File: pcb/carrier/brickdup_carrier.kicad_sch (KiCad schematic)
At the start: 29 parts, among them J1 VBAT IN (JST PH), SW1 PWR SWITCH (JST PH), U1 MP9486A

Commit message: pcb: carrier Cff footprint 0402 -> 0603 for hand-rework
Cff is the designated bench-tuning part (hysteretic ripple injection); 0603
matches the cap kit and human hands. Re-placed + re-routed, DRC 0/0.

Co-Authored-By: Claude Fable 5 <noreply@anthropic.com>
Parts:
- Cff: footprint Capacitor_SMD:C_0402_1005Metric -> Capacitor_SMD:C_0603_1608Metric
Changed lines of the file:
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@@
     (property "Reference" "Cff" (at 232.41 63.49999999999999 0) (effects (font (size 1.27 1.27)) (justify left)))
     (property "Value" "470pF" (at 232.41 66.03999999999999 0) (effects (font (size 1.27 1.27)) (justify left)))
-    (property "Footprint" "Capacitor_SMD:C_0402_1005Metric" (at 229.87 64.77 0) (effects (font (size 1.27 1.27)) (hide yes)))
+    (property "Footprint" "Capacitor_SMD:C_0603_1608Metric" (at 229.87 64.77 0) (effects (font (size 1.27 1.27)) (hide yes)))
     (property "Datasheet" "" (at 229.87 64.77 0) (effects (font (size 1.27 1.27)) (hide yes)))
     (pin "1")

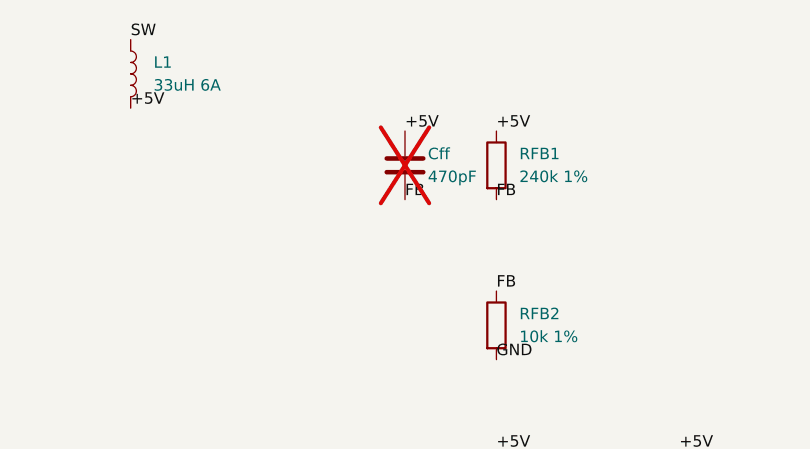
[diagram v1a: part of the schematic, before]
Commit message: pcb: carrier Cff populated by default (470pF 0603, machine-placed)
Zero-hand-SMD build goal: all 24 SMT parts machine-placed incl. Cff; sockets
via JLC THT/hand-solder service (8.5mm height noted); JST wire-loop plug
documented as the solderless SW1 bypass.

Co-Authored-By: Claude Fable 5 <noreply@anthropic.com>
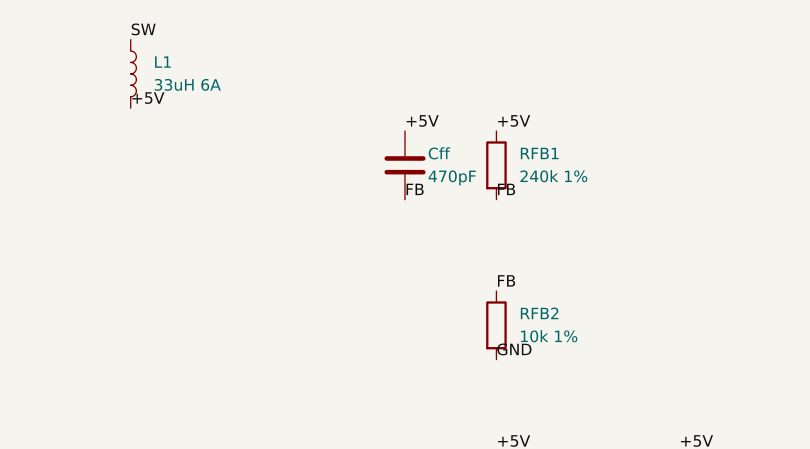
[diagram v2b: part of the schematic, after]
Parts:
- Cff: now fitted
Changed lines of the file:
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@@
     (at 229.87 64.77 0)
     (unit 1)
-    (exclude_from_sim no) (in_bom yes) (on_board yes) (dnp yes)
+    (exclude_from_sim no) (in_bom yes) (on_board yes) (dnp no)
     (property "Reference" "Cff" (at 232.41 63.49999999999999 0) (effects (font (size 1.27 1.27)) (justify left)))
     (property "Value" "470pF" (at 232.41 66.03999999999999 0) (effects (font (size 1.27 1.27)) (justify left)))

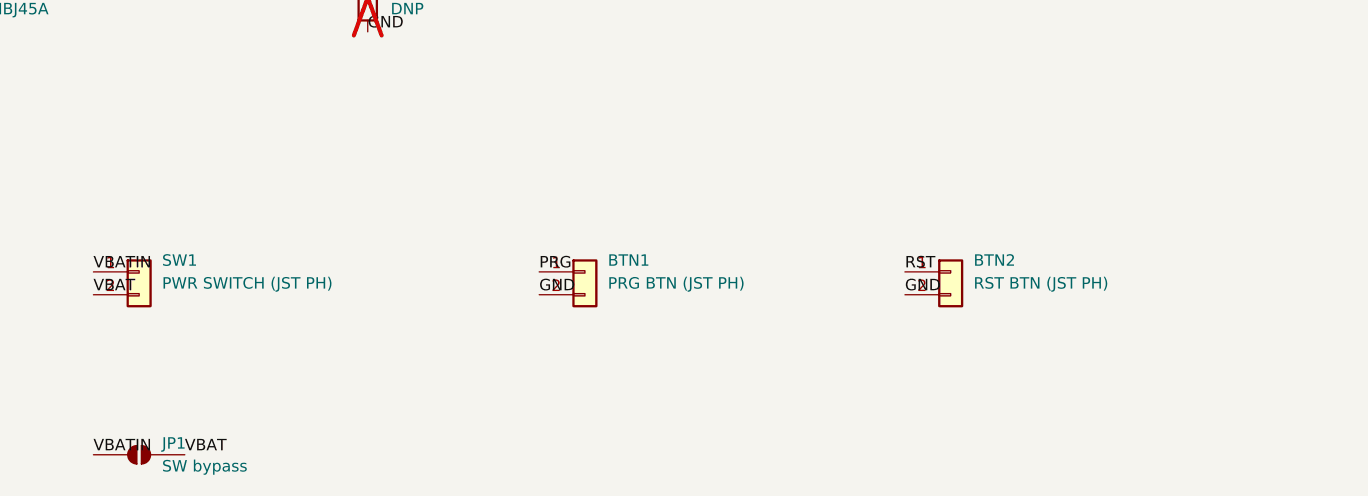
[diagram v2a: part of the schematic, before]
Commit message: pcb: SW1/BTN1/BTN2 -> vertical THT JST (B2B-PH-K-S, C131337)
Top-entry wire exit suits the enclosure (button wires run up to lid
flexures), THT legs are strongest for plug cycles, part is genuine JST,
in stock, and rides the same hand-solder line as the sockets. J1 stays
side-entry facing the LEMO wall. Clip access verified: >=2mm to every
neighbour (BTN2 nudged off the BRK1 row), all fully on-board (edge
exemption now J1 only). Re-routed, DRC 0/0, layout rules pass, full fab
package regenerated (gerbers/BOM/CPL).

Co-Authored-By: Claude Fable 5 <noreply@anthropic.com>
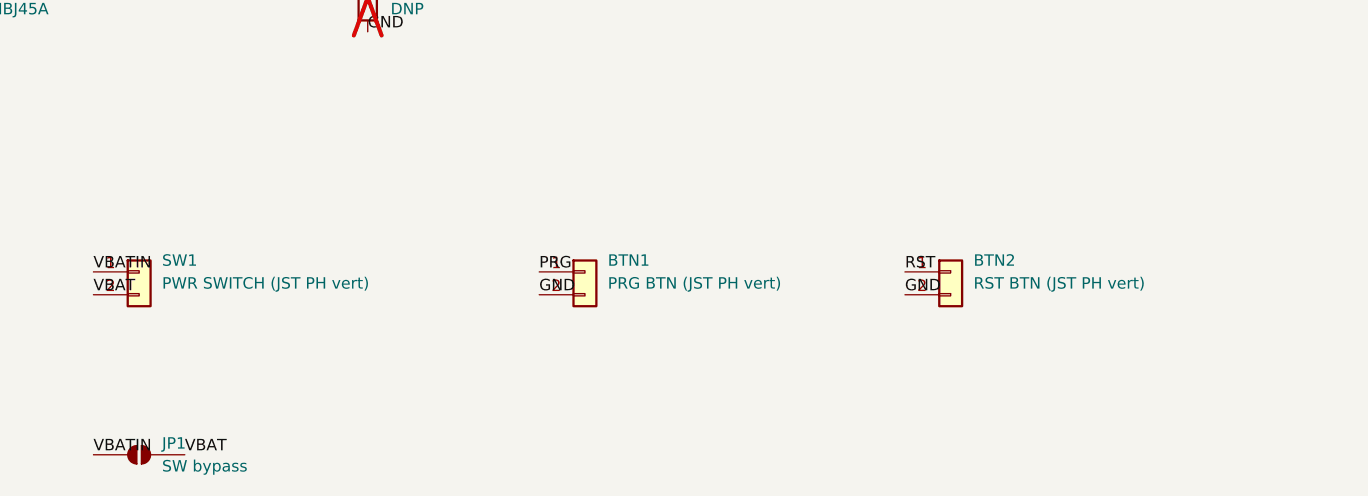
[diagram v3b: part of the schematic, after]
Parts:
- BTN1: value PRG BTN (JST PH) -> PRG BTN (JST PH vert); footprint Connector_JST:JST_PH_S2B-PH-SM4-TB_1x02-1MP_P2.00mm_Horizontal -> Connector_JST:JST_PH_B2B-PH-K_1x02_P2.00mm_Vertical
- BTN2: value RST BTN (JST PH) -> RST BTN (JST PH vert); footprint Connector_JST:JST_PH_S2B-PH-SM4-TB_1x02-1MP_P2.00mm_Horizontal -> Connector_JST:JST_PH_B2B-PH-K_1x02_P2.00mm_Vertical
- SW1: value PWR SWITCH (JST PH) -> PWR SWITCH (JST PH vert); footprint Connector_JST:JST_PH_S2B-PH-SM4-TB_1x02-1MP_P2.00mm_Horizontal -> Connector_JST:JST_PH_B2B-PH-K_1x02_P2.00mm_Vertical
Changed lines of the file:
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@@
     (exclude_from_sim no) (in_bom yes) (on_board yes) (dnp no)
     (property "Reference" "SW1" (at 82.55000000000001 158.75 0) (effects (font (size 1.27 1.27)) (justify left)))
-    (property "Value" "PWR SWITCH (JST PH)" (at 82.55000000000001 161.29000000000002 0) (effects (font (size 1.27 1.27)) (justify left)))
-    (property "Footprint" "Connector_JST:JST_PH_S2B-PH-SM4-TB_1x02-1MP_P2.00mm_Horizontal" (at 80.01 160.02 0) (effects (font (size 1.27 1.27)) (hide yes)))
+    (property "Value" "PWR SWITCH (JST PH vert)" (at 82.55000000000001 161.29000000000002 0) (effects (font (size 1.27 1.27)) (justify left)))
+    (property "Footprint" "Connector_JST:JST_PH_B2B-PH-K_1x02_P2.00mm_Vertical" (at 80.01 160.02 0) (effects (font (size 1.27 1.27)) (hide yes)))
     (property "Datasheet" "" (at 80.01 160.02 0) (effects (font (size 1.27 1.27)) (hide yes)))
     (pin "1")
@@
     (exclude_from_sim no) (in_bom yes) (on_board yes) (dnp no)
     (property "Reference" "BTN1" (at 132.07999999999998 158.75 0) (effects (font (size 1.27 1.27)) (justify left)))
-    (property "Value" "PRG BTN (JST PH)" (at 132.07999999999998 161.29000000000002 0) (effects (font (size 1.27 1.27)) (justify left)))
-    (property "Footprint" "Connector_JST:JST_PH_S2B-PH-SM4-TB_1x02-1MP_P2.00mm_Horizontal" (at 129.54 160.02 0) (effects (font (size 1.27 1.27)) (hide yes)))
+    (property "Value" "PRG BTN (JST PH vert)" (at 132.07999999999998 161.29000000000002 0) (effects (font (size 1.27 1.27)) (justify left)))
+    (property "Footprint" "Connector_JST:JST_PH_B2B-PH-K_1x02_P2.00mm_Vertical" (at 129.54 160.02 0) (effects (font (size 1.27 1.27)) (hide yes)))
     (property "Datasheet" "" (at 129.54 160.02 0) (effects (font (size 1.27 1.27)) (hide yes)))
     (pin "1")
@@
     (exclude_from_sim no) (in_bom yes) (on_board yes) (dnp no)
     (property "Reference" "BTN2" (at 172.72 158.75 0) (effects (font (size 1.27 1.27)) (justify left)))
-    (property "Value" "RST BTN (JST PH)" (at 172.72 161.29000000000002 0) (effects (font (size 1.27 1.27)) (justify left)))
-    (property "Footprint" "Connector_JST:JST_PH_S2B-PH-SM4-TB_1x02-1MP_P2.00mm_Horizontal" (at 170.18 160.02 0) (effects (font (size 1.27 1.27)) (hide yes)))
+    (property "Value" "RST BTN (JST PH vert)" (at 172.72 161.29000000000002 0) (effects (font (size 1.27 1.27)) (justify left)))
+    (property "Footprint" "Connector_JST:JST_PH_B2B-PH-K_1x02_P2.00mm_Vertical" (at 170.18 160.02 0) (effects (font (size 1.27 1.27)) (hide yes)))
     (property "Datasheet" "" (at 170.18 160.02 0) (effects (font (size 1.27 1.27)) (hide yes)))
     (pin "1")
